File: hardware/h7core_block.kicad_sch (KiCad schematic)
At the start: 75 parts, among them J1 USB-C, J3 TC2030-NL SWD, U1 STM32H743VIT6, U107 SP809EK-L-2-9/TR, U3 AP63203WU-7, U4 TLV75533PDBVR, U6 PCM5102APWR, U8 PCM1808PWR, Y1 25MHz 12pF

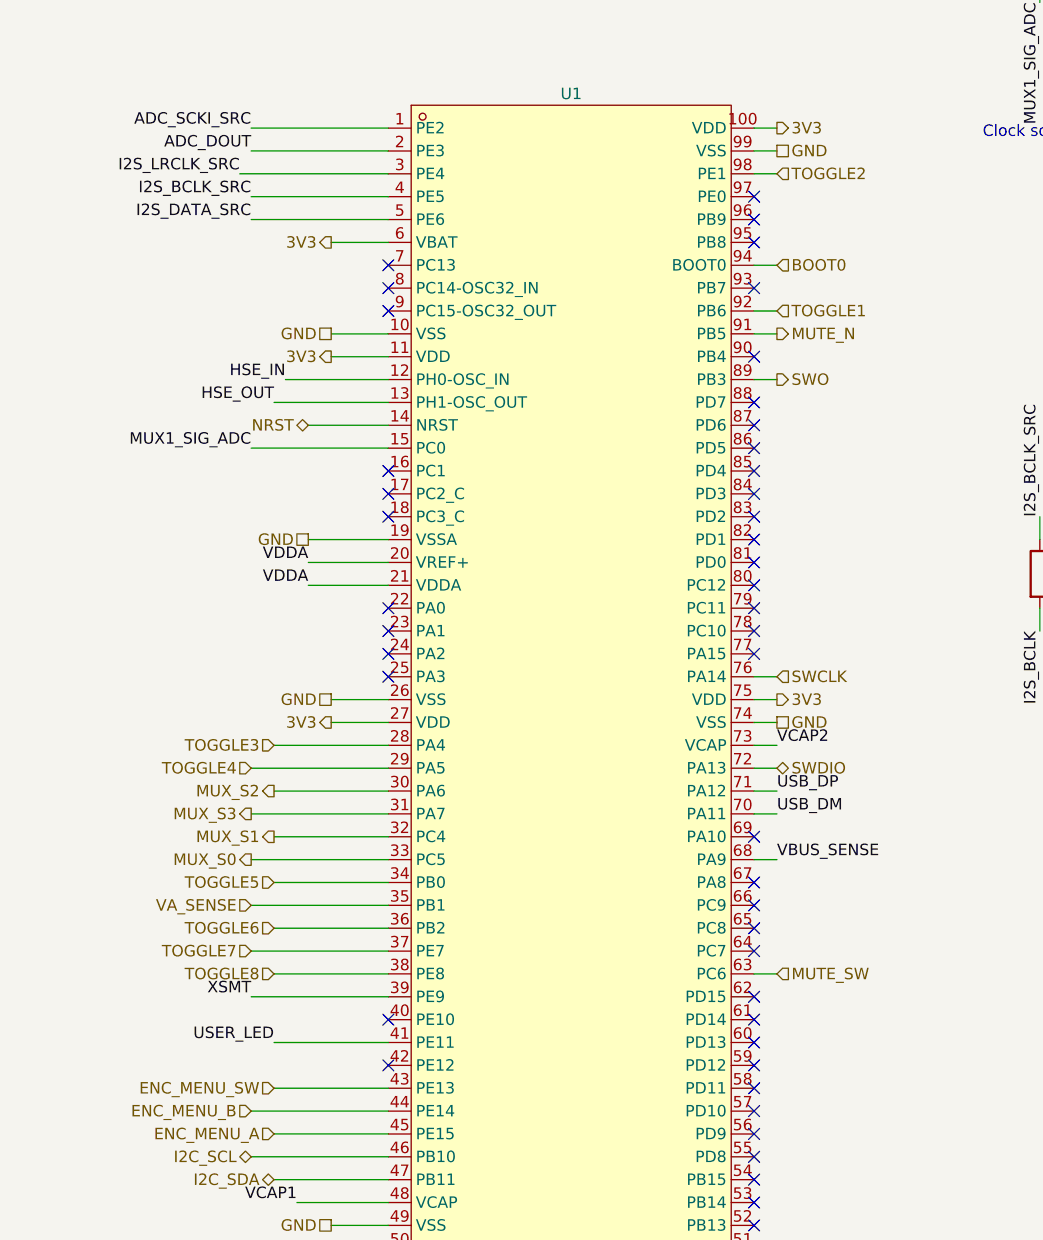
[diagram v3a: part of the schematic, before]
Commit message: feat(sch): move TOGGLE1-8 to U1 east rows, MUX_S to PE8-PE12
U1's east edge interleaved the toggles with MUX_S, VA_SENSE and XSMT, so the toggles had no exit south (commit 2d5c7bc left TOGGLE1-8 unrouted). Pins 28-34, 36, 37 now carry XSMT and the eight toggles in lane order, the MUX selects take PE8-PE12, USER_LED moves to PB7. Firmware pin table and PINMAP follow. Design: hardware/layout/TOGGLE_BUS_BRIEF.md section 2.
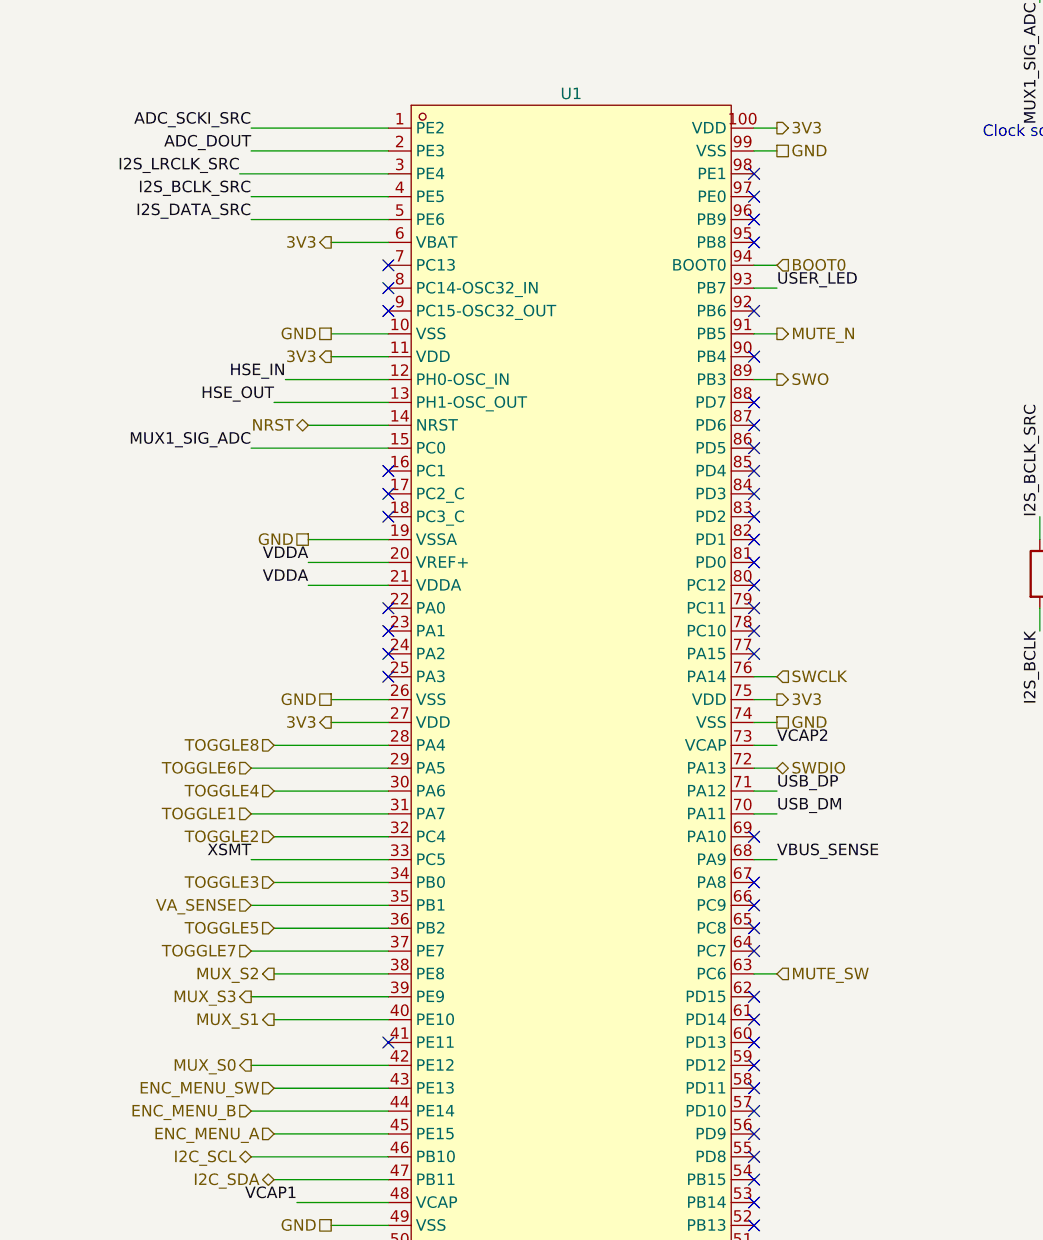
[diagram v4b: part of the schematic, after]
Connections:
- net MUX_S0: now also U1.42 (PE12); no longer U1.33 (PC5)
- net MUX_S1: now also U1.40 (PE10); no longer U1.32 (PC4)
- net MUX_S2: now also U1.38 (PE8); no longer U1.30 (PA6)
- net MUX_S3: now also U1.39 (PE9); no longer U1.31 (PA7)
- net TOGGLE1: now also U1.31 (PA7); no longer U1.92 (PB6)
- net TOGGLE2: now also U1.32 (PC4); no longer U1.98 (PE1)
- net TOGGLE3: now also U1.34 (PB0); no longer U1.28 (PA4)
- net TOGGLE4: now also U1.30 (PA6); no longer U1.29 (PA5)
- net TOGGLE5: now also U1.36 (PB2); no longer U1.34 (PB0)
- net TOGGLE6: now also U1.29 (PA5); no longer U1.36 (PB2)
- net TOGGLE8: now also U1.28 (PA4); no longer U1.38 (PE8)
- net USER_LED: now also U1.93 (PB7); no longer U1.41 (PE11)
- net XSMT: now also U1.33 (PC5); no longer U1.39 (PE9)
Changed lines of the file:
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@@
 	(hierarchical_label "TOGGLE3"
 		(shape input)
-		(at 41.91 146.05 180)
+		(at 41.91 161.29 180)
 		(fields_autoplaced yes)
 		(effects
@@
 	(hierarchical_label "TOGGLE4"
 		(shape input)
-		(at 39.37 148.59 180)
+		(at 41.91 151.13 180)
 		(fields_autoplaced yes)
 		(effects
@@
 	(hierarchical_label "MUX_S2"
 		(shape output)
-		(at 41.91 151.13 180)
+		(at 41.91 171.45 180)
 		(fields_autoplaced yes)
 		(effects
@@
 	(hierarchical_label "MUX_S3"
 		(shape output)
-		(at 39.37 153.67 180)
+		(at 39.37 173.99 180)
 		(fields_autoplaced yes)
 		(effects
@@
 	(hierarchical_label "MUX_S1"
 		(shape output)
-		(at 41.91 156.21 180)
+		(at 41.91 176.53 180)
 		(fields_autoplaced yes)
 		(effects
@@
 	(hierarchical_label "MUX_S0"
 		(shape output)
-		(at 39.37 158.75 180)
+		(at 39.37 181.61 180)
 		(fields_autoplaced yes)
 		(effects
@@
 	(hierarchical_label "TOGGLE5"
 		(shape input)
-		(at 41.91 161.29 180)
+		(at 41.91 166.37 180)
 		(fields_autoplaced yes)
 		(effects
@@
 	(hierarchical_label "TOGGLE6"
 		(shape input)
-		(at 41.91 166.37 180)
+		(at 39.37 148.59 180)
 		(fields_autoplaced yes)
 		(effects
@@
 	(hierarchical_label "TOGGLE8"
 		(shape input)
-		(at 41.91 171.45 180)
+		(at 41.91 146.05 180)
 		(fields_autoplaced yes)
 		(effects
@@
 	)
 	(label "XSMT"
-		(at 39.37 173.99 180)
+		(at 39.37 158.75 180)
 		(fields_autoplaced yes)
 		(effects
@@
 	)
 	(no_connect
-		(at 54.61 176.53)
+		(at 95.25 82.55)
 	)
 	(wire
 		(pts
-			(xy 54.61 179.07) (xy 41.91 179.07)
+			(xy 95.25 95.25) (xy 97.79 95.25)
 		)
 		(stroke
@@
 	)
 	(label "USER_LED"
-		(at 41.91 179.07 180)
+		(at 97.79 95.25 0)
 		(fields_autoplaced yes)
 		(effects
@@
 				(size 1.27 1.27)
 			)
-			(justify right bottom)
+			(justify left bottom)
 		)
 	)
 	(no_connect
-		(at 54.61 181.61)
+		(at 95.25 97.79)
 	)
 	(wire
@@
 	(wire
 		(pts
-			(xy 95.25 97.79) (xy 97.79 97.79)
+			(xy 54.61 181.61) (xy 39.37 181.61)
 		)
 		(stroke
@@
 	(hierarchical_label "TOGGLE1"
 		(shape input)
-		(at 97.79 97.79 0)
+		(at 39.37 153.67 180)
 		(fields_autoplaced yes)
 		(effects
@@
 				(size 1.27 1.27)
 			)
-			(justify left bottom)
+			(justify right bottom)
 		)
 	)
@@
 	(wire
 		(pts
-			(xy 95.25 82.55) (xy 97.79 82.55)
+			(xy 54.61 176.53) (xy 41.91 176.53)
 		)
 		(stroke
@@
 	(hierarchical_label "TOGGLE2"
 		(shape input)
-		(at 97.79 82.55 0)
+		(at 41.91 156.21 180)
 		(fields_autoplaced yes)
 		(effects
@@
 				(size 1.27 1.27)
 			)
-			(justify left bottom)
+			(justify right bottom)
 		)
 	)
@@
 	)
 	(no_connect
-		(at 95.25 95.25)
+		(at 54.61 179.07)
 	)
 	(no_connect

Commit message: feat(sch): pre-fab parts, log gain pot, test points, R7 68k
SMBJ20CA for D105, R158 100k pull-up on LDO_EN, C170 10uF at U6, R7 68k, RVGAIN1 RK09D117000C (15A), TP1-TP5. Per docs/reference/PREFAB_REVIEW_2026-10-08.md.
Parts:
- added C170: 10uF, Capacitor_SMD:C_0805_2012Metric, symbol Device:C
- added R158: 100k, Resistor_SMD:R_0402_1005Metric, symbol Device:R
- added TP5: VBUS, TestPoint:TestPoint_Pad_D1.5mm, symbol Connector:TestPoint
- R7: value 82k -> 68k; LCSC C23254 -> C23231
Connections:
- net 3V3: now also R158.1
- net 3V3A: now also C170.1
- net GND: now also C170.2
- net LDO_EN: now also R158.2
- net VBUS: now also TP5.1

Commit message: feat(hardware): 25 mm gain pot with divider law, relay-switched 1/4" pad
RVGAIN1 becomes the RK09D1130C2P (C361173) wired as a divider: pin 3 on
G2_BOT through R116 470R to G2_RG, new R159 1k from G2_INV to G2_RG, so
the gain knob adds 0 to +30 dB on top of the fixed 20 dB and never
attenuates.

K103 (G6K-2F-Y DC5, same part and driver set as the mute relay K102)
shorts the 25.7 dB 1/4" pad resistors R102 and R105 when de-energised,
so the rest state is MIC and the SM58 on an XLR-to-1/4" cable reaches
the preamp without the pad. PAD_EN on U1 PB8 (high = PEDAL) drives Q102
through R160/R161 with D110 across the coil. K103 pin 5 carries LINE_N
and pin 6 IN_N so the N leg routes on one layer next to R105.

Astra agreed relay over analog switch; packet and reply under
docs/audits.
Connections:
- net PAD_EN: now reaches U1.95 (PB8)
- no-connect marks 50 -> 49
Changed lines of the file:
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@@
 		)
 	)
+	(hierarchical_label "PAD_EN"
+		(shape output)
+		(at 97.79 90.17 0)
+		(fields_autoplaced yes)
+		(effects
+			(font
+				(size 1.27 1.27)
+			)
+			(justify left bottom)
+		)
+	)
+	(wire
+		(pts
+			(xy 95.25 90.17) (xy 97.79 90.17)
+		)
+		(stroke
+			(width 0)
+			(type default)
+		)
+	)
 	(wire
 		(pts
@@
 	)
 	(no_connect
-		(at 95.25 90.17)
-	)
-	(no_connect

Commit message: feat(hardware): pre-fab audit fixes, pad relay K103 routed, rail test pads
PAD_EN on PE11 (pin 41), K103/D110/Q102/R160/R161/R159 placed and routed.
Audit (docs/audits/2026-10-09-prefab-mega-audit.md, tools/mega_audit.py):
one 3V3 copper loop and two acute off-pad Ts cut, 18 bends at pad or via
edges, 29 off-centre ends, 3 split runs, 8 stair-steps re-laid; 12 parts
moved under 0.5 mm. TP6-TP11 on 3V3A, 5V, 5VA, 5VA_W, VREF_BUF, VDDA with
symbols in both sheets (tools/tp_space.py picks the spots). gates.sh ALL
PASS, ERC 0.
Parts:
- added TP11: VDDA, TestPoint:TestPoint_Pad_D1.5mm, symbol Connector:TestPoint
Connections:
- net PAD_EN: now also U1.41 (PE11); no longer U1.95 (PB8)
- net VDDA: now also TP11.1
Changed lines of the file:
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@@
 	(hierarchical_label "PAD_EN"
 		(shape output)
-		(at 97.79 90.17 0)
+		(at 44.45 179.07 180)
 		(fields_autoplaced yes)
 		(effects
@@
 				(size 1.27 1.27)
 			)
-			(justify left bottom)
+			(justify right bottom)
 		)
 	)
 	(wire
 		(pts
-			(xy 95.25 90.17) (xy 97.79 90.17)
+			(xy 54.61 179.07) (xy 44.45 179.07)
 		)
 		(stroke
@@
 	)
 	(no_connect
-		(at 54.61 179.07)
+		(at 95.25 90.17)
 	)
 	(no_connect
@@
 		(fields_autoplaced yes)
 		(effects
+			(font
+				(size 1.27 1.27)
+			)
+			(justify right bottom)
+		)
+	)
+	(symbol
+		(lib_id "Connector:TestPoint")
+		(at 241.3 38.1 0)
+		(unit 1)
+		(exclude_from_sim no)
+		(in_bom no)
+		(on_board yes)
+		(in_pos_files no)
+		(dnp no)
+		(property "Reference" "TP11"
+			(at 245.11 36.83 0)
+			(effects
+				(font
+					(size 1.27 1.27)
+				)
+			)
+		)
+		(property "Value" "VDDA"
+			(at 245.11 39.370000000000005 0)
+			(effects
+				(font
+					(size 1.27 1.27)
+				)
+			)
+		)
+		(property "Footprint" "TestPoint:TestPoint_Pad_D1.5mm"
+			(at 241.3 38.1 0)
+			(hide yes)
+			(effects
+				(font
+					(size 1.27 1.27)
+				)
+			)
+		)
+		(property "Datasheet" "~"
+			(at 241.3 38.1 0)
+			(hide yes)
+			(effects
+				(font
+					(size 1.27 1.27)
+				)
+			)
+		)
+		(pin "1"
+		)
+		(instances
+			(project "cubevox"
+				(path "/99ad1494-2bf8-5051-8886-2c8b83c86254/cdf9c81d-d554-530c-ae51-0929232e7fb3"
+					(reference "TP11")
+					(unit 1)
+				)
+			)
+		)
+	)
+	(wire
+		(pts
+			(xy 241.3 38.1) (xy 241.3 40.64)
+		)
+		(stroke
+			(width 0)
+			(type default)
+		)
+	)
+	(label "VDDA"
+		(at 241.3 40.64 270)
+		(fields_autoplaced yes)
+		(effects

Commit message: fix(hardware): JLC footprints for U107, U108, C19; production v4
The H7 core block came from a KiCad-library project, so U107 (SOT-23),
U108 (SOT-23-5) and C19 (EIA-6032 tantalum) kept stock footprints whose
zero orientation is 180 degrees from JLC's. The v3 CPL therefore had all
three turned round. Each now uses the easyeda2kicad footprint for its
LCSC number (C412495, C221351, C8649) at the same centre; the track
ends, TP10, the U107 ground via and the C19 5 V via follow the 0.13 to
0.30 mm pad shifts. Every assembled asymmetric part is now on a JLC
footprint. gates.sh ALL PASS, mega_audit loops 0, ERC 0.

Production v4: BOM 73 lines / 223 parts, CPL 223 rows, U107 90, U108
180, C19 180 degrees. v2 and v3 are superseded; upload v4 only.
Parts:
- C19: footprint Capacitor_Tantalum_SMD:CP_EIA-6032-28_Kemet-C -> cubevox_h7core:CAP-SMD_L6.0-W3.2-R-RD
- U107: footprint Package_TO_SOT_SMD:SOT-23 -> cubevox_h7core:SOT-23-3_L2.9-W1.6-P1.90-LS2.8-BR
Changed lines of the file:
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@@
 			)
 		)
-		(property "Footprint" "Capacitor_Tantalum_SMD:CP_EIA-6032-28_Kemet-C"
+		(property "Footprint" "cubevox_h7core:CAP-SMD_L6.0-W3.2-R-RD"
 			(at 158.75 190.5 0)
 			(hide yes)
@@
 			)
 		)
-		(property "Footprint" "Package_TO_SOT_SMD:SOT-23"
+		(property "Footprint" "cubevox_h7core:SOT-23-3_L2.9-W1.6-P1.90-LS2.8-BR"
 			(at 298.45 116.84 0)
 			(hide yes)
